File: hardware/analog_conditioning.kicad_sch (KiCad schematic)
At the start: 39 parts, among them J1 AudioJack2, J2 AudioJack2, J4 Conn_02x05_Odd_Even, U1 TL072, U2 TL072, U201 MCP6002-xSN

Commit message: hardware update
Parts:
- renumbered J to J?
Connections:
- net at J?.3 (Pin_3), U1.6 (-), U1.7: now also J?.4 (Pin_4)
- net at J?.7 (Pin_7), U2.6 (-), U2.7: now also J?.8 (Pin_8)
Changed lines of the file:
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@@
 	)
 	(junction
+		(at 172.72 68.58)
+		(diameter 0)
+		(color 0 0 0 0)
+	)
+	(junction
+		(at 172.72 63.5)
+		(diameter 0)
+		(color 0 0 0 0)
+	)
+	(junction
 		(at 228.6 76.2)
 		(diameter 0)
@@
 	(wire
 		(pts
+			(xy 172.72 68.58) (xy 185.42 68.58)
+		)
+		(stroke
+			(width 0)
+			(type default)
+		)
+	)
+	(wire
+		(pts
 			(xy 91.44 123.19) (xy 80.01 123.19)
 		)
@@
 	(wire
 		(pts
+			(xy 172.72 63.5) (xy 185.42 63.5)
+		)
+		(stroke
+			(width 0)
+			(type default)
+		)
+	)
+	(wire
+		(pts
 			(xy 114.3 82.55) (xy 115.57 82.55)
 		)
@@
 		(dnp no)
 		(fields_autoplaced yes)
-		(property "Reference" "#PWR"
+		(property "Reference" "#PWR?"
 			(at 57.15 147.32 0)
 			(effects
@@
 		(pin "1"
 		)
-		(instances)
+		(instances
+			(project "dmx_controller"
+				(path "/c888dd99-01b7-4b4b-82e5-501bcedd41ed/05e4dc0b-bade-45d2-8fa1-6b1ecf425979"
+					(reference "#PWR?")
+					(unit 1)
+				)
+			)
+		)
 	)
 	(symbol
@@
 		(dnp no)
 		(fields_autoplaced yes)
-		(property "Reference" "J"
+		(property "Reference" "J?"
 			(at 179.07 54.61 0)
 			(effects
@@
 		(pin "8"
 		)
-		(instances)
+		(instances
+			(project "dmx_controller"
+				(path "/c888dd99-01b7-4b4b-82e5-501bcedd41ed/05e4dc0b-bade-45d2-8fa1-6b1ecf425979"
+					(reference "J?")
+					(unit 1)
+				)
+			)
+		)
 	)
 	(symbol
@@
 		(dnp no)
 		(fields_autoplaced yes)
-		(property "Reference" "#PWR"
+		(property "Reference" "#PWR?"
 			(at 57.15 124.46 0)
 			(effects
@@
 		(pin "1"
 		)
-		(instances)
+		(instances
+			(project "dmx_controller"
+				(path "/c888dd99-01b7-4b4b-82e5-501bcedd41ed/05e4dc0b-bade-45d2-8fa1-6b1ecf425979"
+					(reference "#PWR?")
+					(unit 1)
+				)
+			)
+		)
 	)
 )

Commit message: hardware update
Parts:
- removed C1, C4: 4n7, Capacitor_SMD:C_0805_2012Metric, symbol Device:C
- removed C10, C7: 1u, Capacitor_SMD:CP_Elec_4x5.4, symbol Device:C_Polarized
- removed C11, C12, C2, C5, C8, C9: 220n, Capacitor_SMD:C_0805_2012Metric, symbol Device:C
- removed C203: 5n6, Capacitor_SMD:C_0805_2012Metric, symbol Device:C
- removed C3, C6: 33u, Capacitor_SMD:CP_Elec_6.3x5.8, symbol Device:C_Polarized
- removed D1, D2, D3, D4: D, Diode_SMD:D_SOD-323_HandSoldering, symbol Device:D
- removed J1, J2: AudioJack2, Connector_Audio:Jack_6.35mm_Neutrik_NMJ6HFD2-AU_Horizontal, symbol Connector_Audio:AudioJack2
- removed J?: Conn_02x05_Odd_Even, Connector_IDC:IDC-Header_2x05_P2.54mm_Vertical, symbol Connector_Generic:Conn_02x05_Odd_Even
- removed R1, R4, R5, R8: 1M, Resistor_SMD:R_0805_2012Metric, symbol Device:R_US
- removed R2, R6: 22k, Resistor_SMD:R_0805_2012Metric, symbol Device:R_US
- removed R3, R7: 3k9, Resistor_SMD:R_0805_2012Metric, symbol Device:R_US
- removed U1, U2: TL072, Package_SO:SOIC-8_3.9x4.9mm_P1.27mm, symbol Amplifier_Operational:TL072
- added C201, C205, C206: 5n6, Capacitor_SMD:C_0805_2012Metric, symbol Device:C
- added C207, C208: 3n3, Capacitor_SMD:C_0805_2012Metric, symbol Device:C
- added J202: Conn_02x05_Odd_Even, Connector_IDC:IDC-Header_2x05_P2.54mm_Vertical, symbol Connector_Generic:Conn_02x05_Odd_Even
- added R205, R211, R214: 7k15, Resistor_SMD:R_0805_2012Metric, symbol Device:R_US
- added R206, R207, R208, R209, R212, R215, R216: 10k, Resistor_SMD:R_0805_2012Metric, symbol Device:R_US
- added R210, R213: 2k61, Resistor_SMD:R_0805_2012Metric, symbol Device:R_US
- added RV201, RV202: R_Potentiometer, symbol Device:R_Potentiometer
- added U201, U202: TL072, Package_SO:SOIC-8_3.9x4.9mm_P1.27mm, symbol Amplifier_Operational:TL072
- C204: now not fitted
- R203: value 2k61 -> 10k
- R204: value 7k15 -> 2k61; now not fitted
- renumbered C201 to C202, C202 to C203, J4 to J201, U201 to U203
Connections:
- net +12V: now also J202.10 (Pin_10), J202.9 (Pin_9)
- net +3.3V: now also J202.8 (Pin_8)
- net -12V: now also J202.1 (Pin_1), J202.2 (Pin_2)
- net GND: now also C207.2, C208.2, J202.5 (Pin_5), J202.6 (Pin_6), R208.2, R216.2, RV201.3, RV202.3
- net adc3_0: no longer C202.2, U203.1, U203.2 (-)
- net adc3_1: no longer U203.6 (-), U203.7
- net analog_in_1: now also RV201.1; no longer R201.1
- net analog_in_2: now also RV202.1; no longer R203.1
- net at R203.2: now also U203.3 (+), R206.1; no longer R204.1
- net at C203.1, R202.2: now also C204.1, R205.2, U201.5 (+); no longer U203.3 (+)
- net at C202.1, R201.2, R202.1: now also R204.2, C201.1, R205.1
- new net: R209.2, R212.2, R215.2, R216.1, U203.5 (+), U203.6 (-)
- new net: C205.1, C206.1, R210.2, R211.1, R213.2, R214.1
- new net: C207.1, C208.1, R211.2, R214.2, U202.5 (+)
- new net: C205.2, C206.2, R212.1, U202.6 (-), U202.7
- new net: C201.2, C202.2, R203.1, U201.6 (-), U201.7
- new net: R210.1, R213.1, U202.1, U202.2 (-)
- new net: RV202.2, U202.3 (+)
- new net: R207.2, R208.1, U203.2 (-)
- new net: R201.1, R204.1, U201.1, U201.2 (-)
- new net: RV201.2, U201.3 (+)
- new net V_REF_1_65V: J202.4 (Pin_4), R206.2, R209.1
- new net analog_out_1: J202.3 (Pin_3), R207.1, U203.1
- new net analog_out_2: J202.7 (Pin_7), R215.1, U203.7
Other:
- moved on the sheet: C202, C203, J201, R201, R202, U203A, U203B, U203C

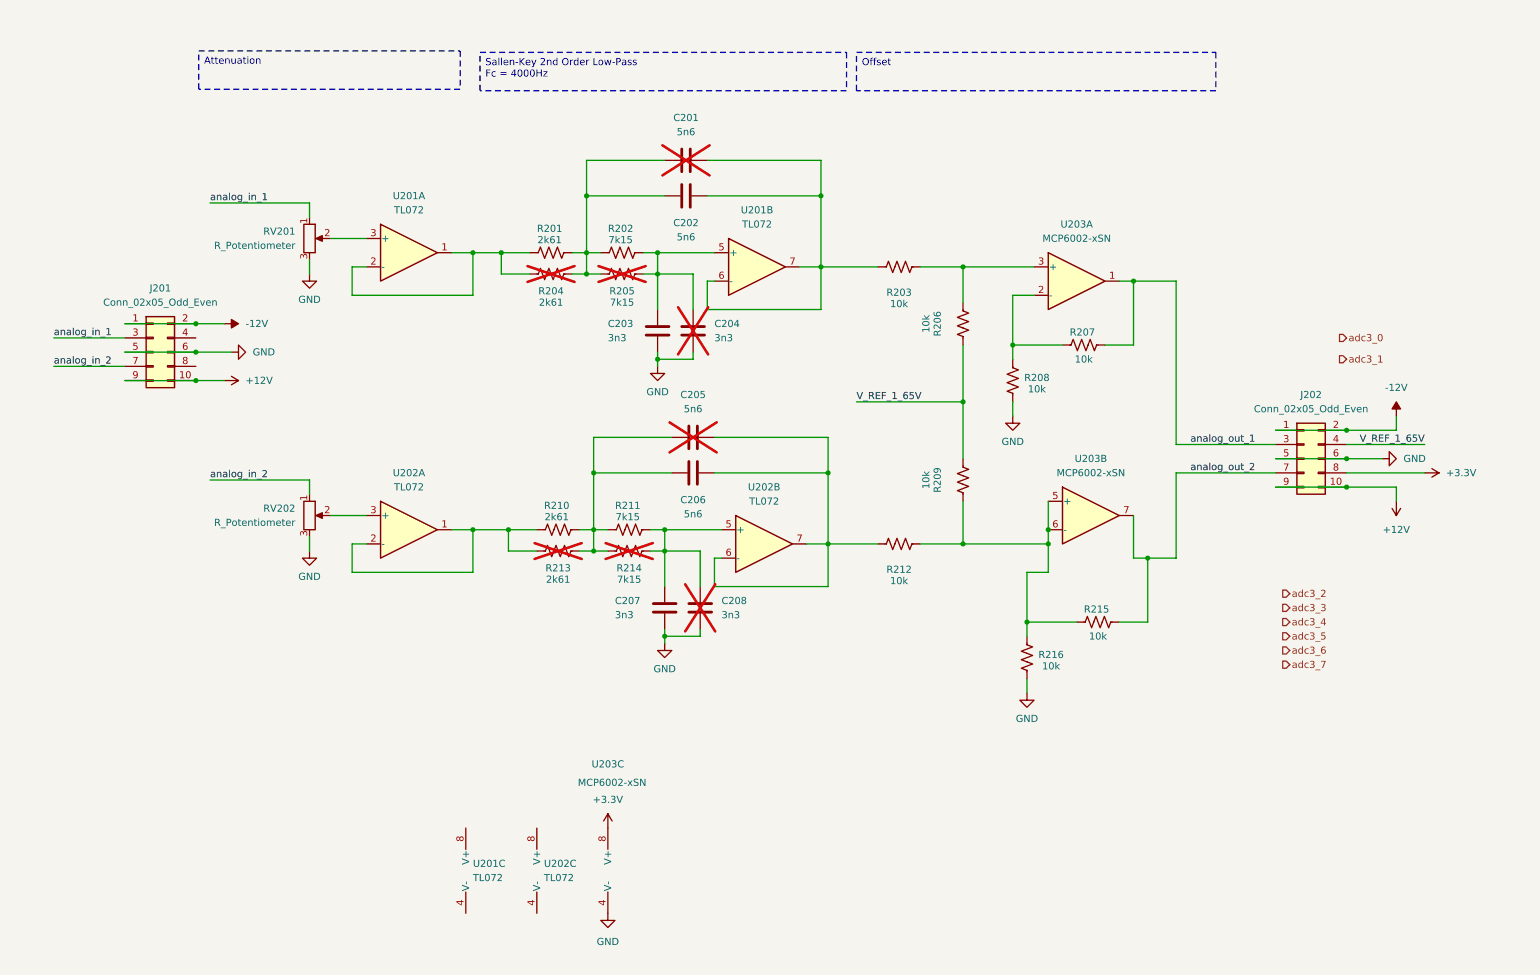
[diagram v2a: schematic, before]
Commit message: analog conditioning and preamp board sent for prototype manufacture
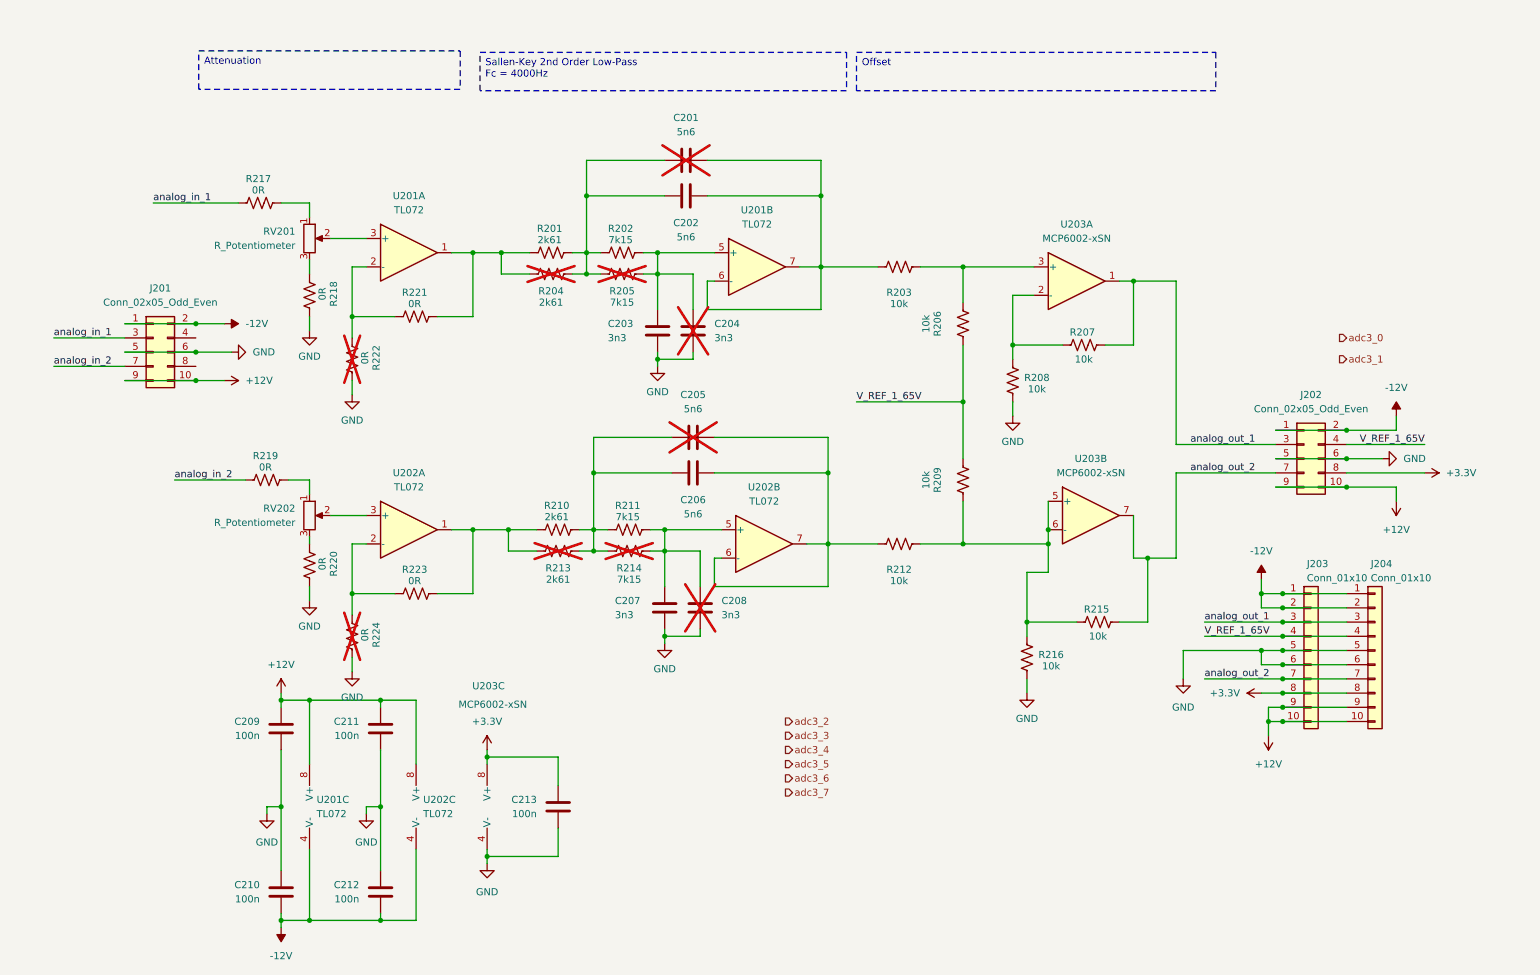
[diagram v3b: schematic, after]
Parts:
- added C209, C210, C211, C212, C213: 100n, Capacitor_SMD:C_0805_2012Metric, symbol Device:C
- added J203, J204: Conn_01x10, Connector_PinHeader_2.54mm:PinHeader_1x10_P2.54mm_Vertical, symbol Connector_Generic:Conn_01x10
- added R217, R218, R219, R220, R221, R222, R223, R224: 0R, Resistor_SMD:R_0805_2012Metric, symbol Device:R_US
- RV201, RV202: footprint (none) -> Potentiometer_THT:Potentiometer_Bourns_3296W_Vertical
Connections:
- net +12V: now also U201.8 (V+), U202.8 (V+), C209.2, C211.2, J203.10 (Pin_10), J203.9 (Pin_9), J204.10 (Pin_10), J204.9 (Pin_9)
- net +3.3V: now also C213.2, J203.8 (Pin_8), J204.8 (Pin_8)
- net -12V: now also U201.4 (V-), U202.4 (V-), C210.1, C212.1, J203.1 (Pin_1), J203.2 (Pin_2), J204.1 (Pin_1), J204.2 (Pin_2)
- net GND: now also C209.1, C210.2, C211.1, C212.2, C213.1, J203.5 (Pin_5), J203.6 (Pin_6), J204.5 (Pin_5), J204.6 (Pin_6), R218.2, R220.2, R222.2, R224.2; no longer RV201.3, RV202.3
- net V_REF_1_65V: now also J203.4 (Pin_4), J204.4 (Pin_4)
- net analog_in_1: now also R217.1; no longer RV201.1
- net analog_in_2: now also R219.1; no longer RV202.1
- net analog_out_1: now also J203.3 (Pin_3), J204.3 (Pin_3)
- net analog_out_2: now also J203.7 (Pin_7), J204.7 (Pin_7)
- net at R210.1, R213.1, U202.1: now also R223.2; no longer U202.2 (-)
- net at R201.1, R204.1, U201.1: now also R221.2; no longer U201.2 (-)
- new net: R221.1, R222.1, U201.2 (-)
- new net: R220.1, RV202.3
- new net: R217.2, RV201.1
- new net: R219.2, RV202.1
- new net: R218.1, RV201.3
- new net: R223.1, R224.1, U202.2 (-)
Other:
- moved on the sheet: U201C, U202C, U203C
